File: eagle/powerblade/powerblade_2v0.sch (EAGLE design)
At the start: 91 parts, among them J21 JTAG_14PIN_IDC-NL, J23 AC_INSLOT_OUT, Q1 2N7002, Q2 2N7002, Q3 2N7002, Q4 BF2040, U1 MAX9910, U2 MAX9910, U3 NCS2200S, U4 MSP430FR5738, U5 LP2980, U6 KL02, X1 32.768kHz, X2 32.768kHz, Y1 ANT-USP

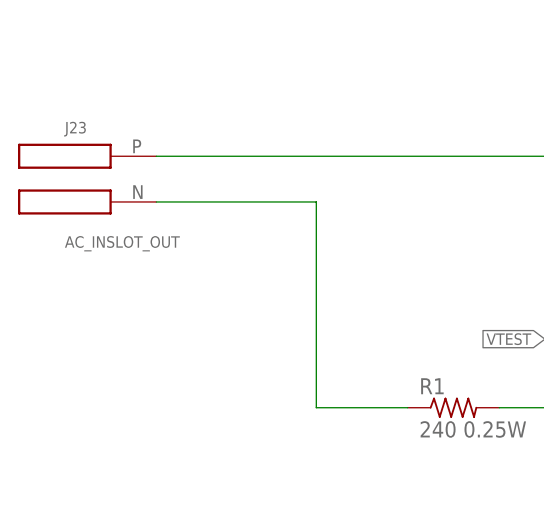
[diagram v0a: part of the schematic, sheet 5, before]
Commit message: updated to 3 prong ac
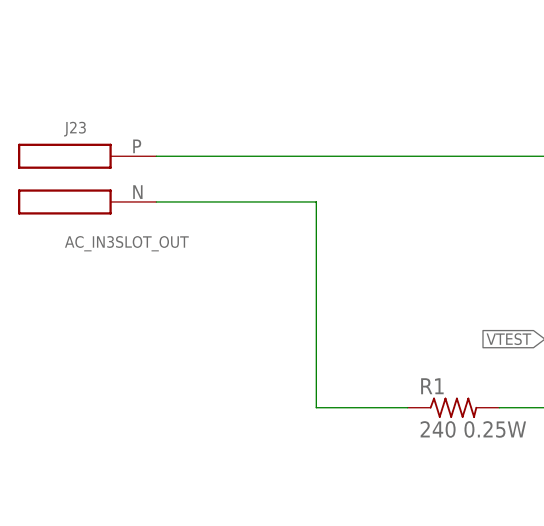
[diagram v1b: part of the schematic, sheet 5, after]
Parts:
- J23: value AC_INSLOT_OUT -> AC_IN3SLOT_OUT; device powerfilm:AC_INSLOT_OUT -> powerfilm:AC_IN3SLOT_OUT
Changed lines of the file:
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@@
 <part name="+3V7" library="supply1" deviceset="+3V3" device=""/>
 <part name="GND22" library="supply1" deviceset="GND" device=""/>
-<part name="J23" library="powerfilm" deviceset="AC_IN" device="SLOT_OUT" value="AC_INSLOT_OUT">
+<part name="J23" library="powerfilm" deviceset="AC_IN" device="3SLOT_OUT" value="AC_IN3SLOT_OUT">
 <attribute name="DIGIKEY" value="3M11307-ND"/>
 </part>
